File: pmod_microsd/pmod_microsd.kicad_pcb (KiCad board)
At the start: 4 copper layers, 25.4 x 15.2 mm, 23 parts, among them J1 PZ254R-12-12P, J2 Micro_SD_Card_Det2, U1 RCLAMP0524P, U2 RCLAMP0524P, U3 AIP74LVC1T45GB236TR

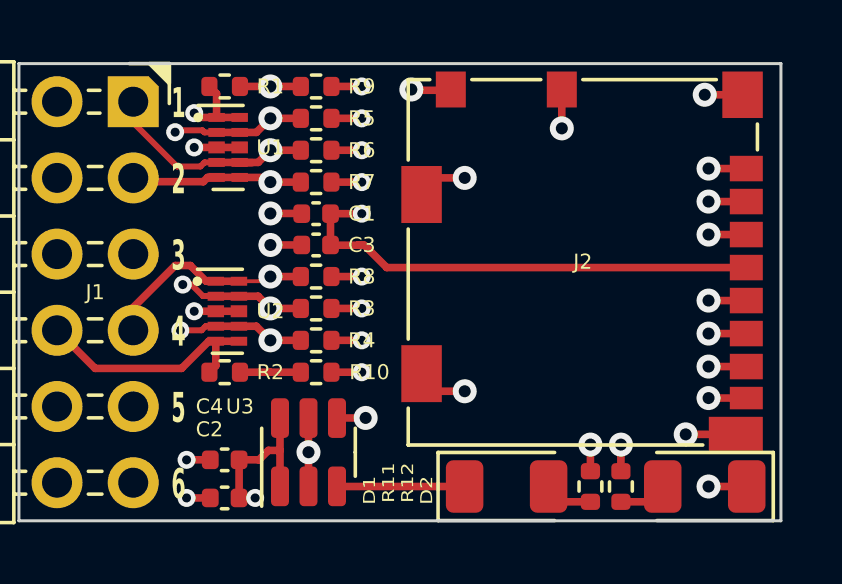
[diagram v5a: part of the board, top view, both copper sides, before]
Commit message: pmod_microsd/*.kicad_pcb: improved GND vias
- Add random vias for GND layer, improve PI and SI

Signed-off-by: Huang Rui <vowstar@gmail.com>
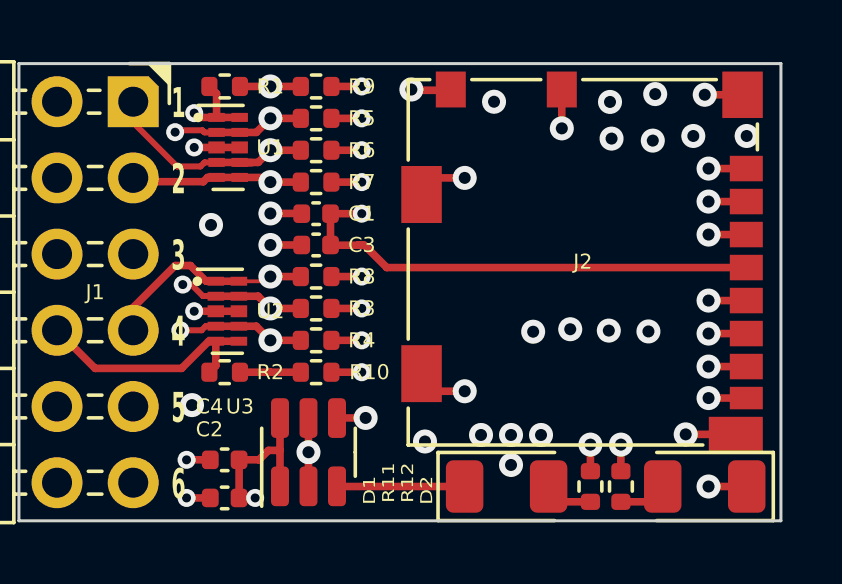
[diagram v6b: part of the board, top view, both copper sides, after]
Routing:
- net GND: vias 14 -> 32
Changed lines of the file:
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@@
   (segment (start 110.692703 122.541968) (end 109.842703 122.541968) (width 0.254) (layer "F.Cu") (net 10))
   (via (at 105.485703 124.573968) (size 0.8) (drill 0.4) (layers "F.Cu" "B.Cu") (remove_unused_layers) (keep_end_layers) (zone_layer_connections) (net 10))
+  (via (at 116.962469 114.186748) (size 0.8) (drill 0.4) (layers "F.Cu" "B.Cu") (free) (net 10))
   (via (at 118.820703 125.716968) (size 0.8) (drill 0.4) (layers "F.Cu" "B.Cu") (remove_unused_layers) (keep_end_layers) (zone_layer_connections) (net 10))
   (via (at 118.058703 123.978968) (size 0.8) (drill 0.4) (layers "F.Cu" "B.Cu") (remove_unused_layers) (keep_end_layers) (zone_layer_connections) (net 10))
+  (via (at 101.602508 123.002955) (size 0.8) (drill 0.4) (layers "F.Cu" "B.Cu") (free) (net 10))
   (via (at 110.692703 115.429968) (size 0.8) (drill 0.4) (layers "F.Cu" "B.Cu") (remove_unused_layers) (keep_end_layers) (zone_layer_connections) (net 10))
   (via (at 118.693703 112.658968) (size 0.8) (drill 0.4) (layers "F.Cu" "B.Cu") (remove_unused_layers) (keep_end_layers) (zone_layer_connections) (net 10))
+  (via (at 109.368777 124.216231) (size 0.8) (drill 0.4) (layers "F.Cu" "B.Cu") (free) (net 10))
+  (via (at 114.210658 120.474187) (size 0.8) (drill 0.4) (layers "F.Cu" "B.Cu") (free) (net 10))
+  (via (at 118.312703 114.032968) (size 0.8) (drill 0.4) (layers "F.Cu" "B.Cu") (free) (net 10))
+  (via (at 112.236443 123.998968) (size 0.8) (drill 0.4) (layers "F.Cu" "B.Cu") (free) (net 10))
+  (via (at 111.670306 112.891735) (size 0.8) (drill 0.4) (layers "F.Cu" "B.Cu") (free) (net 10))
+  (via (at 102.236443 116.998968) (size 0.8) (drill 0.4) (layers "F.Cu" "B.Cu") (free) (net 10))
   (via (at 101.421703 126.097968) (size 0.6) (drill 0.3) (layers "F.Cu" "B.Cu") (remove_unused_layers) (keep_end_layers) (zone_layer_connections) (net 10))
+  (via (at 115.58774 114.119881) (size 0.8) (drill 0.4) (layers "F.Cu" "B.Cu") (free) (net 10))
   (via (at 104.215703 117.665848) (size 0.8) (drill 0.4) (layers "F.Cu" "B.Cu") (remove_unused_layers) (keep_end_layers) (zone_layer_connections) (net 10))
+  (via (at 120.090703 114.032968) (size 0.8) (drill 0.4) (layers "F.Cu" "B.Cu") (free) (net 10))
   (via (at 101.675703 114.414027) (size 0.6) (drill 0.3) (layers "F.Cu" "B.Cu") (remove_unused_layers) (keep_end_layers) (zone_layer_connections) (net 10))
+  (via (at 111.236443 123.998968) (size 0.8) (drill 0.4) (layers "F.Cu" "B.Cu") (free) (net 10))
+  (via (at 115.536292 112.898142) (size 0.8) (drill 0.4) (layers "F.Cu" "B.Cu") (free) (net 10))
+  (via (at 117.042703 112.635968) (size 0.8) (drill 0.4) (layers "F.Cu" "B.Cu") (free) (net 10))
   (via (at 118.820703 120.618968) (size 0.8) (drill 0.4) (layers "F.Cu" "B.Cu") (remove_unused_layers) (keep_end_layers) (zone_layer_connections) (net 10))
+  (via (at 116.817072 120.547969) (size 0.8) (drill 0.4) (layers "F.Cu" "B.Cu") (free) (net 10))
   (via (at 101.675703 119.874968) (size 0.6) (drill 0.3) (layers "F.Cu" "B.Cu") (remove_unused_layers) (keep_end_layers) (zone_layer_connections) (net 10))
+  (via (at 112.236443 124.998968) (size 0.8) (drill 0.4) (layers "F.Cu" "B.Cu") (free) (net 10))
+  (via (at 112.974795 120.557011) (size 0.8) (drill 0.4) (layers "F.Cu" "B.Cu") (free) (net 10))
   (via (at 110.692703 122.541968) (size 0.8) (drill 0.4) (layers "F.Cu" "B.Cu") (remove_unused_layers) (keep_end_layers) (zone_layer_connections) (net 10))
   (via (at 104.215703 116.6153) (size 0.8) (drill 0.4) (layers "F.Cu" "B.Cu") (remove_unused_layers) (keep_end_layers) (zone_layer_connections) (net 10))
   (via (at 101.421703 124.827968) (size 0.6) (drill 0.3) (layers "F.Cu" "B.Cu") (remove_unused_layers) (keep_end_layers) (zone_layer_connections) (net 10))
+  (via (at 113.236443 123.998968) (size 0.8) (drill 0.4) (layers "F.Cu" "B.Cu") (free) (net 10))
   (via (at 113.929703 113.778968) (size 0.8) (drill 0.4) (layers "F.Cu" "B.Cu") (remove_unused_layers) (keep_end_layers) (zone_layer_connections) (net 10))
+  (via (at 115.496356 120.519532) (size 0.8) (drill 0.4) (layers "F.Cu" "B.Cu") (free) (net 10))
   (segment (start 106.441203 125.716968) (end 106.435703 125.711468) (width 0.254) (layer "F.Cu") (net 11))
   (segment (start 110.689703 125.716968) (end 106.441203 125.716968) (width 0.254) (layer "F.Cu") (net 11))
@@
     )
   )
+  (group "ViaStitching GND" (id 23d9fcf4-aef4-4f3a-9ed5-7c522a93b2c7)
+    (members
+      0560e1a5-adb6-4408-baaa-f29dbe41fb24
+      1aab477f-1242-49b6-8bac-5c35cfb61f44
+      276bccbd-945b-44ca-a99c-fcaf8101a876
+      29b54971-a56b-4c9c-8cb1-6bbdde8b3303
+      3681ced3-bc8d-4a80-a728-f7e1d4a0dc4a
+      41ce0870-8b66-455a-8272-03a5b2d28f06
+      477acbaa-116a-4d69-8ffa-cd2e9c94d43e
+      7fad2775-5d75-4e07-af55-afa2f5401039
+      91b085c8-2c2c-454c-816f-e89cc6b5f1d6
+      9533991a-2652-4282-a517-35588022ff31
+      9f1541f2-9e9a-4dc6-bdbc-87b7a5f12b88
+      b1ea72ef-4e50-4742-a465-7e5e201e1663
+      b83050fe-6853-4006-baac-c12857221bb4
+      e82da56a-ca91-4384-a0cb-8b35e8b12a35
+      eba2bae1-7251-419e-a615-6e0a320e8bc1
+    )
+  )

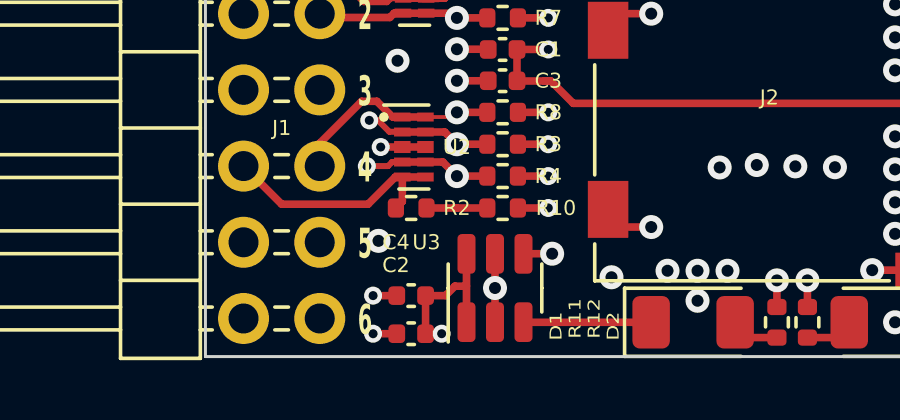
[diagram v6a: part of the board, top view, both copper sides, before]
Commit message: pmod_microsd: Migrate to kicad8
- Migrate schematics to kicad8
- Migrate PCB to kicad8
- Clean ERC
- Clean LVS and DRC

Signed-off-by: Huang Rui <vowstar@gmail.com>
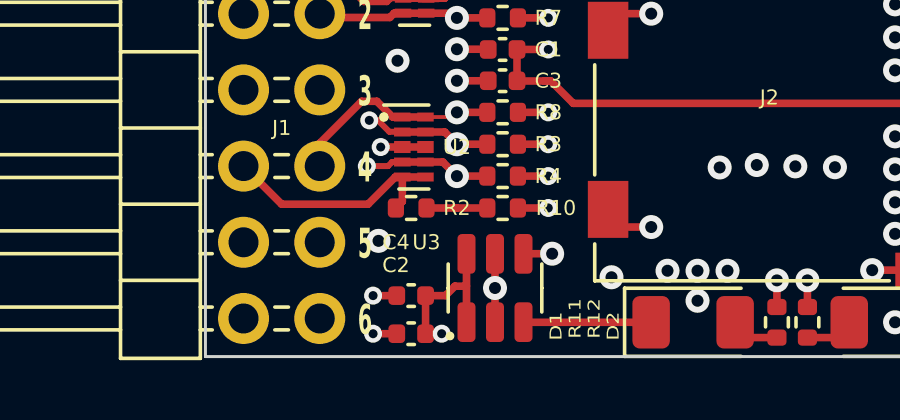
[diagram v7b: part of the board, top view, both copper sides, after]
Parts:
- U3: footprint Package_TO_SOT_SMD:SOT-23-6 -> CHIPSAlliance_Package_TO_SOT_SMD:SOT-23-6
